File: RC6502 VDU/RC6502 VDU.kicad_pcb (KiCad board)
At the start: 2 copper layers, 99.1 x 99.7 mm, 34 parts, among them J1 RC6502_Backplane, J2 VDU_BASE, J3 VIDEO, J4 Hole, J5 Hole, J6 Hole, J7 Hole, J8 RCA_PLUG, U1 MC6847, U10 74LS02, U11 VDU_Port, U12 74LS374, U2 HM62256BLP-7, U3 74LS244, U4 74LS244, U5 74LS245, U6 74LS374, U7 74HCT138, U8 74LS32, U9 74HCT138, X1 3.579545 MHz

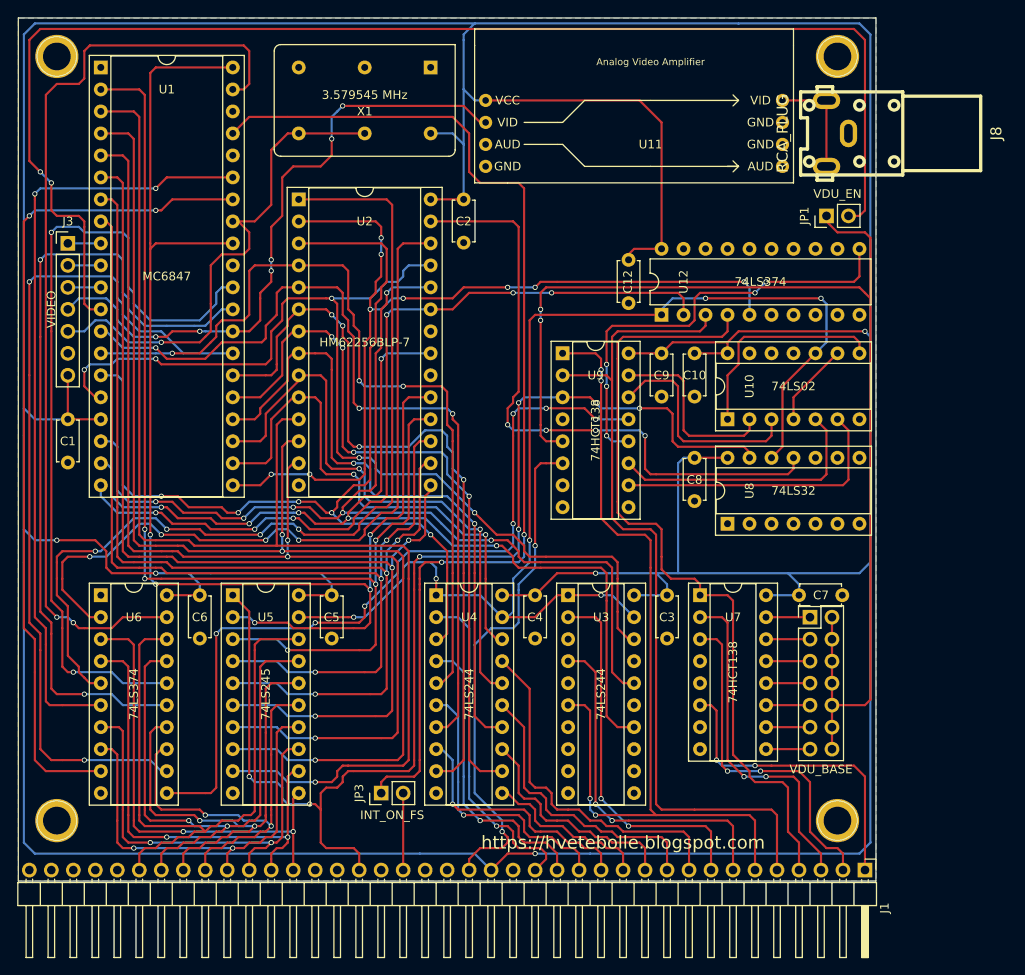
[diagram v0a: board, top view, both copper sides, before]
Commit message: Updated layout to include changes
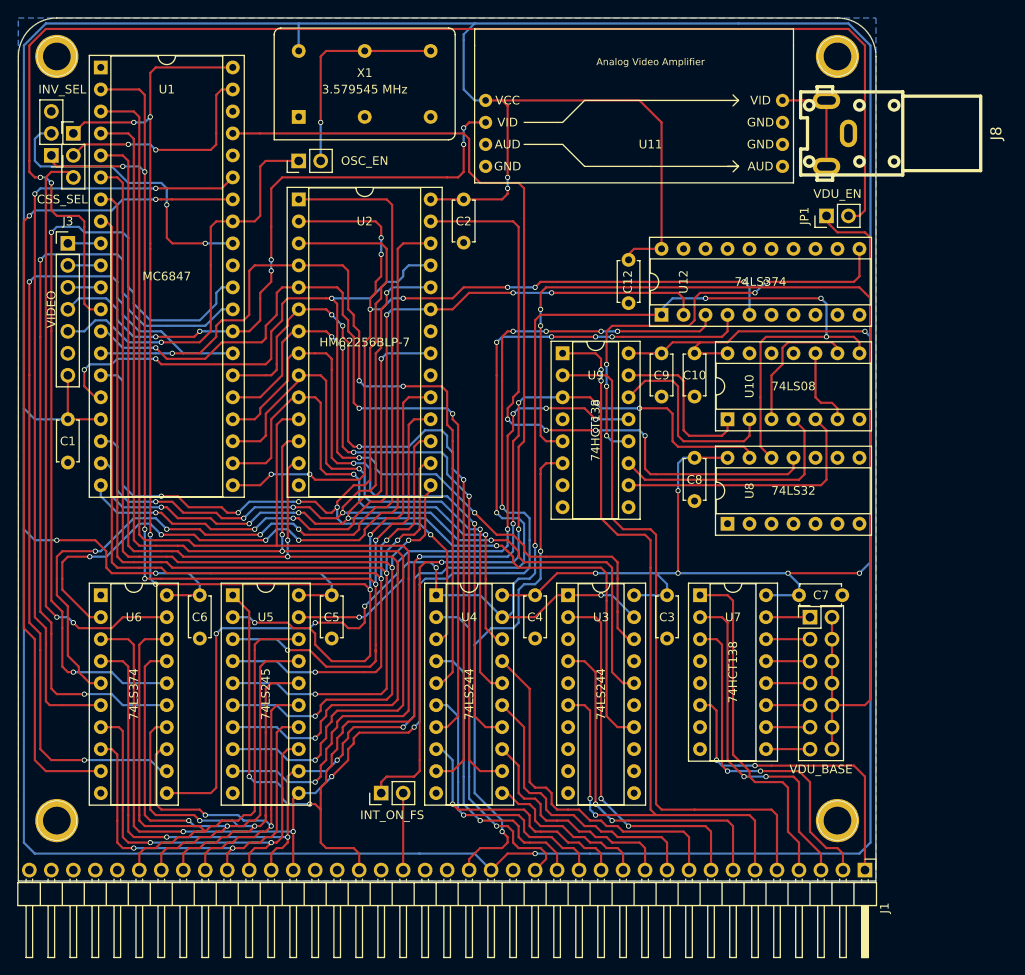
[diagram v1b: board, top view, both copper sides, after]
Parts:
- added JP2: OSC_EN, Pin_Headers:Pin_Header_Straight_1x02_Pitch2.54mm, F.Cu at (85.1, 61.0)
- added JP4: CSS_SEL, Pin_Headers:Pin_Header_Straight_1x03_Pitch2.54mm, F.Cu at (59.1, 57.8)
- added JP5: INV_SEL, Pin_Headers:Pin_Header_Straight_1x03_Pitch2.54mm, F.Cu at (56.5, 60.3)
- U10: value 74LS02 -> 74LS08
- U12: footprint Housings_DIP:DIP-20_W7.62mm -> Housings_DIP:DIP-20_W7.62mm_Socket
- moved X1 16.3 mm to (85.1, 55.9), turned to 0 degrees
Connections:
- U1 pad 32: VD7 -> Net-(JP5-Pad2)
- U1 pad 39: CSS -> Net-(JP4-Pad2)
- U10 pad 10: ~CS_RAM_EXT -> Net-(U10-Pad10)
- U10 pad 11: GND -> (no net)
- U10 pad 13: (no net) -> GND
- U10 pad 6: Net-(U10-Pad6) -> Net-(U10-Pad10)
- U10 pad 8: Net-(U10-Pad1) -> ~CS_RAM_EXT
- U10 pad 9: Net-(U10-Pad4) -> Net-(U10-Pad3)
- U12 pad 3: A11 -> D0
- U12 pad 4: A12 -> D1
- U9 pad 10: Net-(U10-Pad6) -> Net-(U10-Pad5)
- U9 pad 11: Net-(U10-Pad5) -> Net-(U10-Pad4)
- U9 pad 14: Net-(U10-Pad3) -> Net-(U10-Pad2)
- U9 pad 15: Net-(U10-Pad2) -> Net-(U10-Pad1)
- X1 pad 8: VDU_CLK -> Net-(JP2-Pad2)
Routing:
- net D1: track 54.7 -> 158.0 mm, vias 2 -> 9
- net D0: track 52.9 -> 155.1 mm, vias 2 -> 9
- net A12: track 91.9 -> 40.2 mm
- net CSS: track 108.6 -> 68.8 mm
- net Net-(JP5-Pad2): track 0.00 -> 34.9 mm, vias 0 -> 2
- net Net-(U10-Pad6): track 33.2 -> 0.00 mm
- net Net-(JP4-Pad2): track 0.00 -> 25.4 mm, vias 0 -> 2
- net Net-(JP2-Pad2): track 0.00 -> 25.0 mm, vias 0 -> 1
- net Net-(U10-Pad4): track 9.72 -> 28.2 mm
- net A11: track 97.4 -> 79.7 mm
- net VD6: track 136.0 -> 150.8 mm, vias 5 -> 7
- net VDU_CLK: track 59.6 -> 48.0 mm
- net ~CS_RAM_EXT: track 141.7 -> 152.6 mm, vias 6 -> 7
- net Net-(U10-Pad10): track 0.00 -> 9.42 mm
- net Net-(U10-Pad3): track 25.7 -> 16.3 mm
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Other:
- outline, holes or cut-outs redrawn
- board text added: "CSS_SEL"
- board text added: "CSS_SEL 1-2 D7 2-3 REG0 b7 (CSS)"
- board text added: "INT_ON_FS"
- board text added: "INV_SEL"
- board text added: "INV_SEL 1-2 D6 2-3 OFF"
- board text added: "OSC_EN"
- board text added: "RC6502 VDU Revision B"
- board text added: "Register 0 ($x800): [b0,1] Page select [b2] G/~A [b03] S/~A [b04] GM2 [b05] GM1 [b06] GM0 [b07] CSS"
- board text added: "Register 1 ($xC00): [b0,1] Video RAM Window Select (external access)"
- board text added: "VDU Clock NTSC freq. oscillator (Only with B/W)"
- board text removed: "RC6502 VDU Board Revision A https://hvetebolle.blogspot.com"
- board text removed: "Register 0: [b0,1] Page select [b2] G/~A [b03] S/~A [b04] GM2 [b05] GM1 [b06] GM0 [b07] CSS"
- board text removed: "Register 1: [b0,1] Video RAM Window Select (external access)"
- board text removed: "VDU Clock NTSC freq. oscillator"

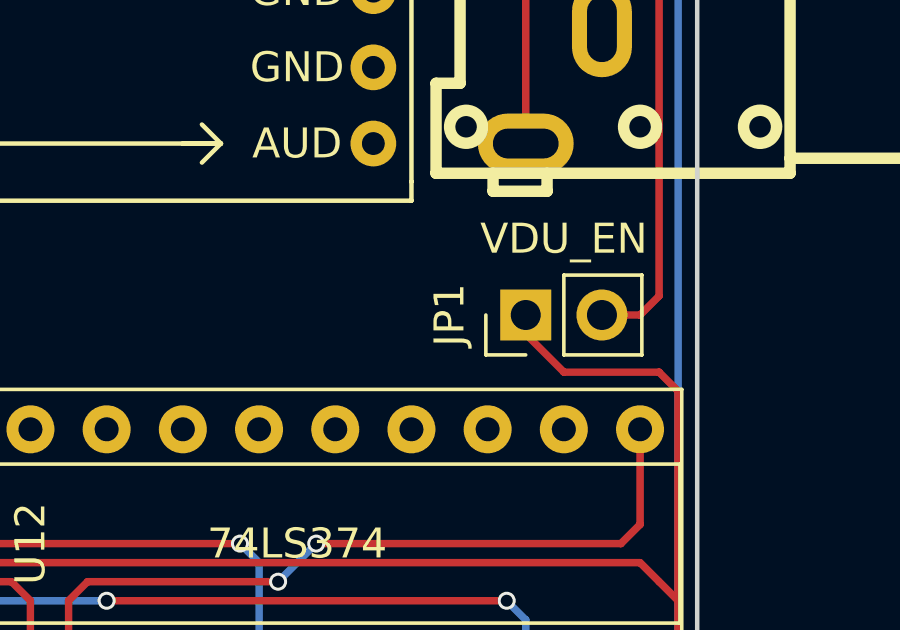
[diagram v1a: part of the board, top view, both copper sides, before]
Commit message: VDU silkscreen tweaks
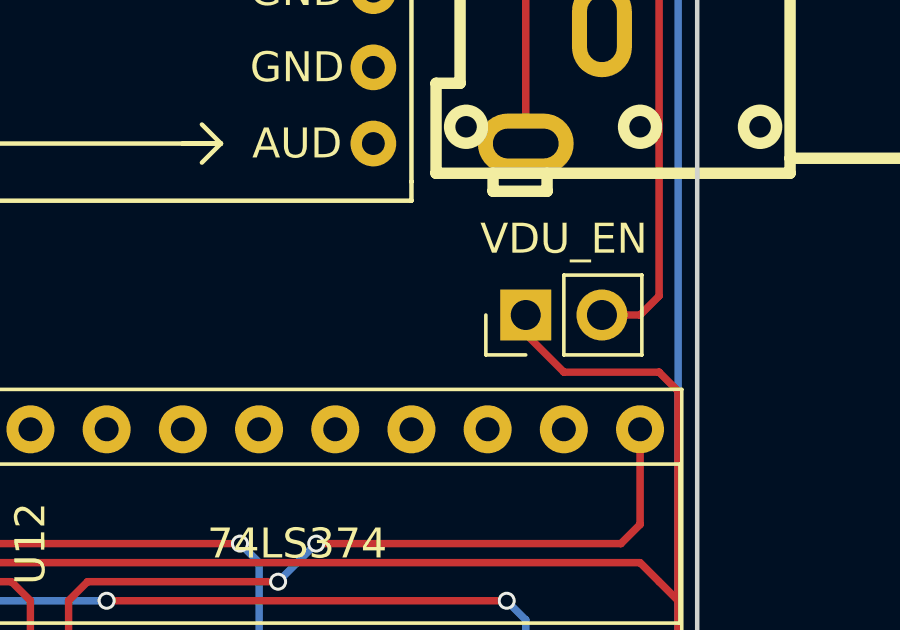
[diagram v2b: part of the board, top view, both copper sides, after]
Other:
- board text added: "VDU_EN"
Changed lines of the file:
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@@
     (area 52.629999 44.374999 151.840001 144.220001)
     (thickness 1.6)
-    (drawings 97)
+    (drawings 103)
     (tracks 1993)
     (zones 0)
@@
       (effects (font (thickness 0.3048)))
     )
-    (fp_text value RCA_PLUG (at 0 -8.89 90) (layer F.Fab)
+    (fp_text value RCA_PLUG (at 6.35 8.255 180) (layer F.Fab)
       (effects (font (thickness 0.3048)))
     )
@@
     (descr "Through hole straight pin header, 1x02, 2.54mm pitch, single row")
     (tags "Through hole pin header THT 1x02 2.54mm single row")
-    (fp_text reference JP1 (at 0 -2.54 270) (layer F.SilkS)
+    (fp_text reference JP1 (at 0 -2.54 90) (layer F.Fab)
       (effects (font (size 1 1) (thickness 0.15)))
     )
@@
     )
   )
+  (gr_text VDU_EN (at 147.32 64.77) (layer B.SilkS)
+    (effects (font (size 1 1) (thickness 0.15)) (justify mirror))
+  )
+  (gr_line (start 146.05 67.31) (end 148.59 67.31) (angle 90) (layer B.SilkS) (width 0.2))
+  (gr_line (start 144.145 69.215) (end 144.145 65.405) (angle 90) (layer B.SilkS) (width 0.2))
+  (gr_line (start 150.495 69.215) (end 144.145 69.215) (angle 90) (layer B.SilkS) (width 0.2))
+  (gr_line (start 150.495 65.405) (end 150.495 69.215) (angle 90) (layer B.SilkS) (width 0.2))
+  (gr_line (start 144.145 65.405) (end 150.495 65.405) (angle 90) (layer B.SilkS) (width 0.2))
   (gr_line (start 52.705 48.895) (end 52.705 144.145) (angle 90) (layer Edge.Cuts) (width 0.15))
   (gr_line (start 151.765 48.895) (end 151.765 144.145) (angle 90) (layer Edge.Cuts) (width 0.15))
